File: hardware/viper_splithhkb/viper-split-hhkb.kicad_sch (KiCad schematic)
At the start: 131 parts, among them SW1 SW_Push, SW10 SW_Push, SW11 SW_Push, SW12 SW_Push, SW13 SW_Push, SW14 SW_Push, SW14_1 SW_Push, SW15 SW_Push, SW16 SW_Push, SW17 SW_Push, SW18 SW_Push, SW19 SW_Push, SW2 SW_Push, SW20 SW_Push, SW21 SW_Push, SW22 SW_Push, SW23 SW_Push, SW24 SW_Push, SW25 SW_Push, SW26 SW_Push, SW27 SW_Push, SW28 SW_Push, SW29 SW_Push, SW29_1 SW_Push, SW3 SW_Push, SW30 SW_Push, SW31 SW_Push, SW32 SW_Push, SW33 SW_Push, SW34 SW_Push, SW35 SW_Push, SW36 SW_Push, SW37 SW_Push, SW38 SW_Push, SW39 SW_Push, SW4 SW_Push, SW40 SW_Push, SW41 SW_Push, SW42 SW_Push, SW43 SW_Push, SW43_1 SW_Push, SW44 SW_Push, SW45 SW_Push, SW46 SW_Push, SW47 SW_Push, SW48 SW_Push, SW49 SW_Push, SW5 SW_Push, SW50 SW_Push, SW51 SW_Push, SW52 SW_Push, SW53 SW_Push, SW54 SW_Push, SW55 SW_Push, SW55_1 SW_Push, SW56 SW_Push, SW57 SW_Push, SW58 SW_Push, SW59 SW_Push, SW59_1 SW_Push, SW6 SW_Push, SW60 SW_Push, SW61 SW_Push, SW62 SW_Push, SW63 SW_Push, SW7 SW_Push, SW8 SW_Push, SW9 SW_Push

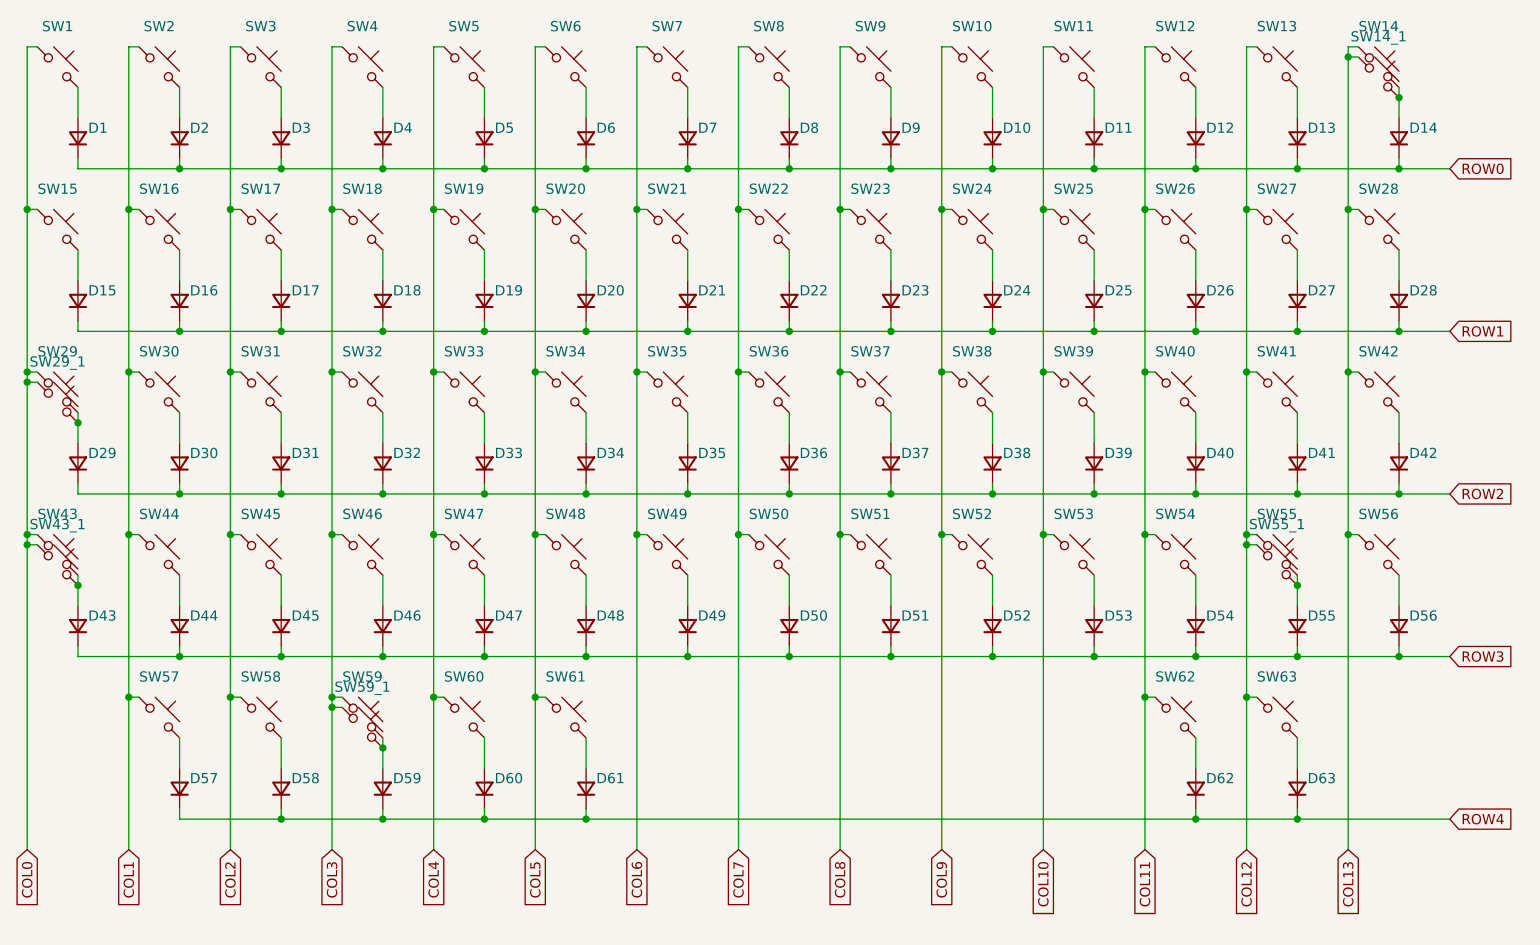
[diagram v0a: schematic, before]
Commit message: Manually corrected split-hhkb layout
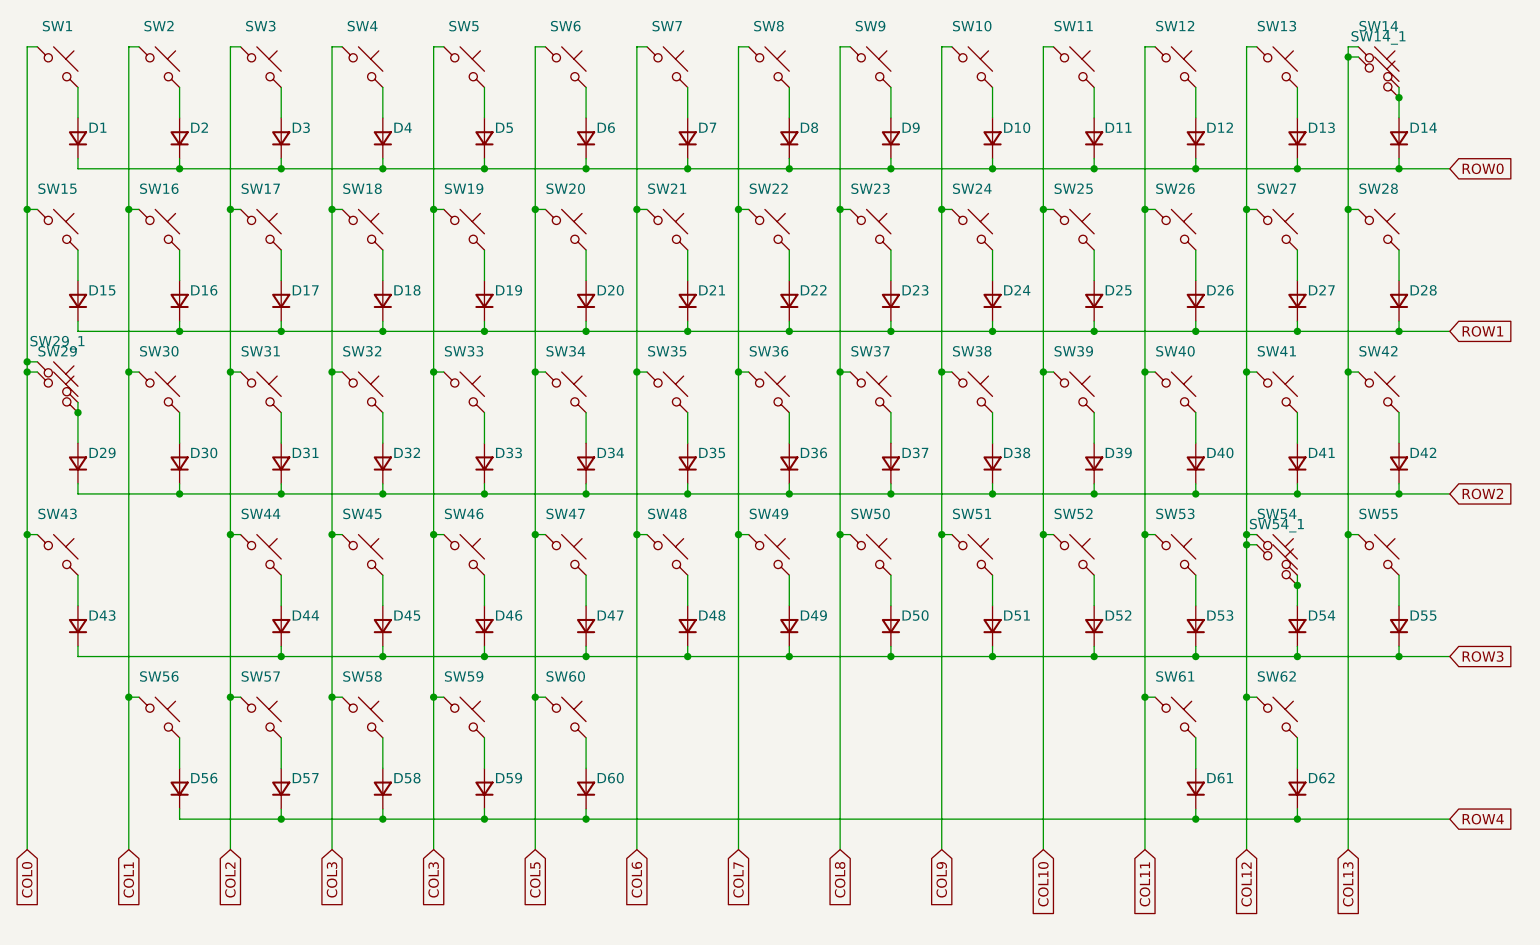
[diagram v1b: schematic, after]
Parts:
- removed D63: D, Diode_SMD:D_SOD-123F, symbol Device:D_Small
- removed SW43_1, SW55_1, SW59_1, SW63: SW_Push, Switch_Keyboard_Hybrid:SW_Hybrid_Cherry_MX_Alps_1.00u, symbol Switch:SW_Push_45deg
- added SW54_1: SW_Push, PCM_Switch_Keyboard_Hybrid:SW_Hybrid_Cherry_MX_Alps_1.75u, symbol Switch:SW_Push_45deg
- D1, D10, D11, D12, D13, D14, D15, D16, D17, D18, D19, D2, D20, D21, D22, D23, D24, D25, D26, D27, D28, D29, D3, D30, D31, D32, D33, D34, D35, D36, D37, D38, D39, D4, D40, D41, D42, D43, D44, D45, D46, D47, D48, D49, D5, D50, D51, D52, D53, D54, D55, D56, D57, D58, D59, D6, D60, D61, D62, D7, D8, D9: footprint Diode_SMD:D_SOD-123F -> Diode_SMD:D_0805_2012Metric_Pad1.15x1.40mm_HandSolder
- SW1, SW10, SW11, SW12, SW13, SW14_1, SW16, SW17, SW18, SW19, SW2, SW20, SW21, SW22, SW23, SW24, SW25, SW26, SW27, SW3, SW30, SW31, SW32, SW33, SW34, SW35, SW36, SW37, SW38, SW39, SW4, SW40, SW42, SW44, SW45, SW46, SW47, SW48, SW49, SW5, SW50, SW51, SW52, SW53, SW55, SW56, SW6, SW62, SW7, SW8, SW9: footprint Switch_Keyboard_Hybrid:SW_Hybrid_Cherry_MX_Alps_1.00u -> PCM_Switch_Keyboard_Hybrid:SW_Hybrid_Cherry_MX_Alps_1.00u
- SW14: footprint Switch_Keyboard_Hybrid:SW_Hybrid_Cherry_MX_Alps_1.00u -> PCM_Switch_Keyboard_Hybrid:SW_Hybrid_Cherry_MX_Alps_2.00u
- SW15, SW28, SW57, SW61: footprint Switch_Keyboard_Hybrid:SW_Hybrid_Cherry_MX_Alps_1.00u -> PCM_Switch_Keyboard_Hybrid:SW_Hybrid_Cherry_MX_Alps_1.50u
- SW29: footprint Switch_Keyboard_Hybrid:SW_Hybrid_Cherry_MX_Alps_1.00u -> PCM_Switch_Keyboard_Hybrid:SW_Hybrid_Cherry_MX_Alps_1.75u
- SW29_1: footprint Switch_Keyboard_Hybrid:SW_Hybrid_Cherry_MX_Alps_1.00u -> PCM_Switch_Keyboard_Hybrid:SW_Hybrid_Cherry_MX_Alps_1.25u
- SW41, SW43: footprint Switch_Keyboard_Hybrid:SW_Hybrid_Cherry_MX_Alps_1.00u -> PCM_Switch_Keyboard_Hybrid:SW_Hybrid_Cherry_MX_Alps_2.25u
- SW54: footprint Switch_Keyboard_Hybrid:SW_Hybrid_Cherry_MX_Alps_1.00u -> PCM_Switch_Keyboard_Hybrid:SW_Hybrid_Cherry_MX_Alps_2.75u
- SW58, SW60: footprint Switch_Keyboard_Hybrid:SW_Hybrid_Cherry_MX_Alps_1.00u -> PCM_Switch_Keyboard_Hybrid:SW_Hybrid_Cherry_MX_Alps_3.00u
- SW59: footprint Switch_Keyboard_Hybrid:SW_Hybrid_Cherry_MX_Alps_1.00u -> PCM_Switch_Keyboard_Hybrid:SW_Hybrid_Cherry_MX_Alps_7.00u
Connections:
- net COL1: now also SW56.1; no longer SW44.1, SW57.1
- net COL10: now also SW52.1; no longer SW53.1
- net COL11: now also SW53.1, SW61.1; no longer SW54.1, SW62.1
- net COL12: now also SW54.1, SW62.1, SW54_1.1; no longer SW55.1
- net COL13: now also SW55.1; no longer SW56.1
- net COL2: now also SW44.1, SW57.1; no longer SW45.1, SW58.1
- net COL3: now also SW19.1, SW33.1, SW45.1, SW5.1, SW58.1
- net COL5: now also SW47.1, SW60.1; no longer SW48.1, SW61.1
- net COL6: now also SW48.1; no longer SW49.1
- net COL7: now also SW49.1; no longer SW50.1
- net COL8: now also SW50.1; no longer SW51.1
- net COL9: now also SW51.1; no longer SW52.1
- net ROW3: no longer D56.1 (K)
- net ROW4: now also D56.1 (K)
- net at D54.2 (A), SW54.2: now also SW54_1.2
- removed net COL4: SW19.1, SW33.1, SW47.1, SW5.1, SW60.1
